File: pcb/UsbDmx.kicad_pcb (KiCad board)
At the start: 2 copper layers, 100 x 100 mm, 101 parts, among them CON101 10PIN_ISP_AVR, CON201 XLR3_F_GROUND, CON202 XLR3_M_GROUND, J101 USB_B, J102 Barrel_Jack, Q201 BC817, Q202 BC817, Q203 BC807, Q204 BC817, Q205 BC817, U101 74LS573, U102 USBN9604-28M, U103 AS6C6264, U104 L7805, U105 ATMEGA8515-16AU, U106 USBLC6-2SC6, U201 SN75176, U202 6N137, U203 6N137, U204 AM2D-0505SZ, U205 SN75176, Y101 24MHz

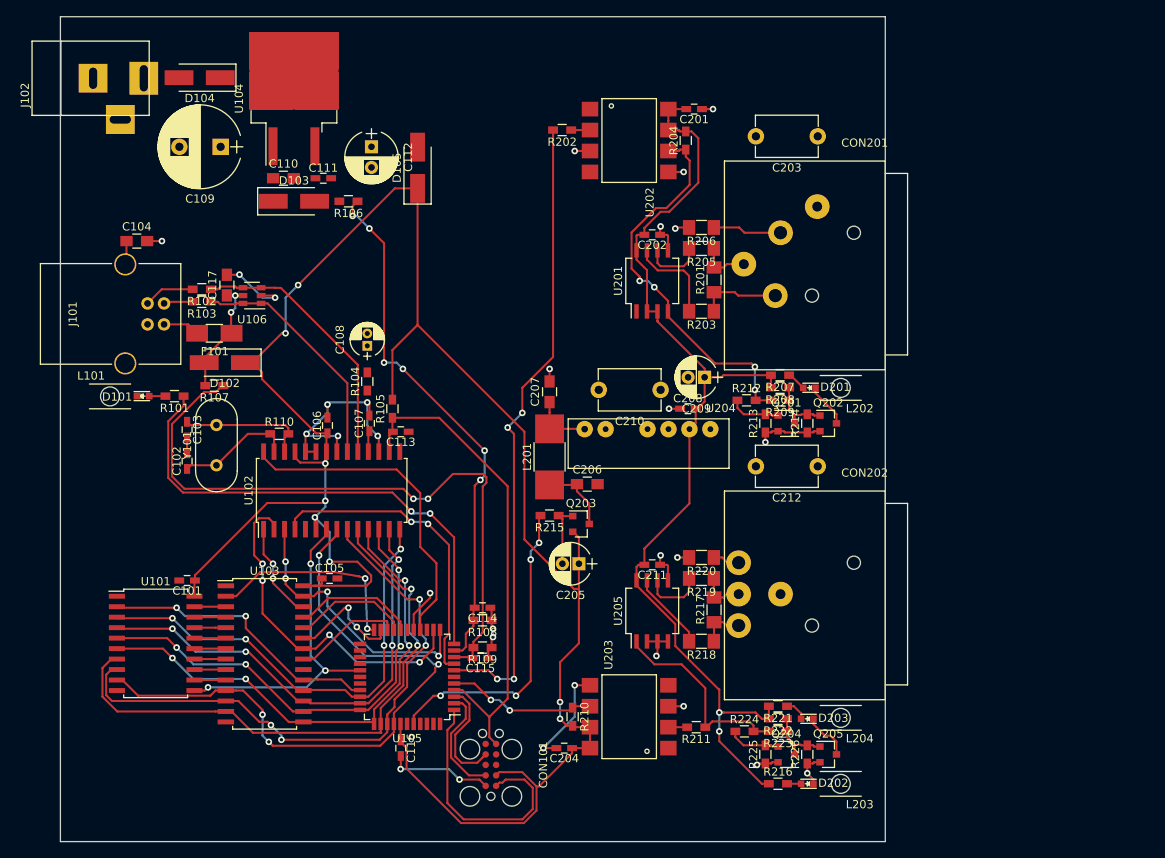
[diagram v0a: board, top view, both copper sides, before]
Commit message: Finished layout
Added esd protection diodes to the dmx interface
Routed everything
added ground planes
added some logos...
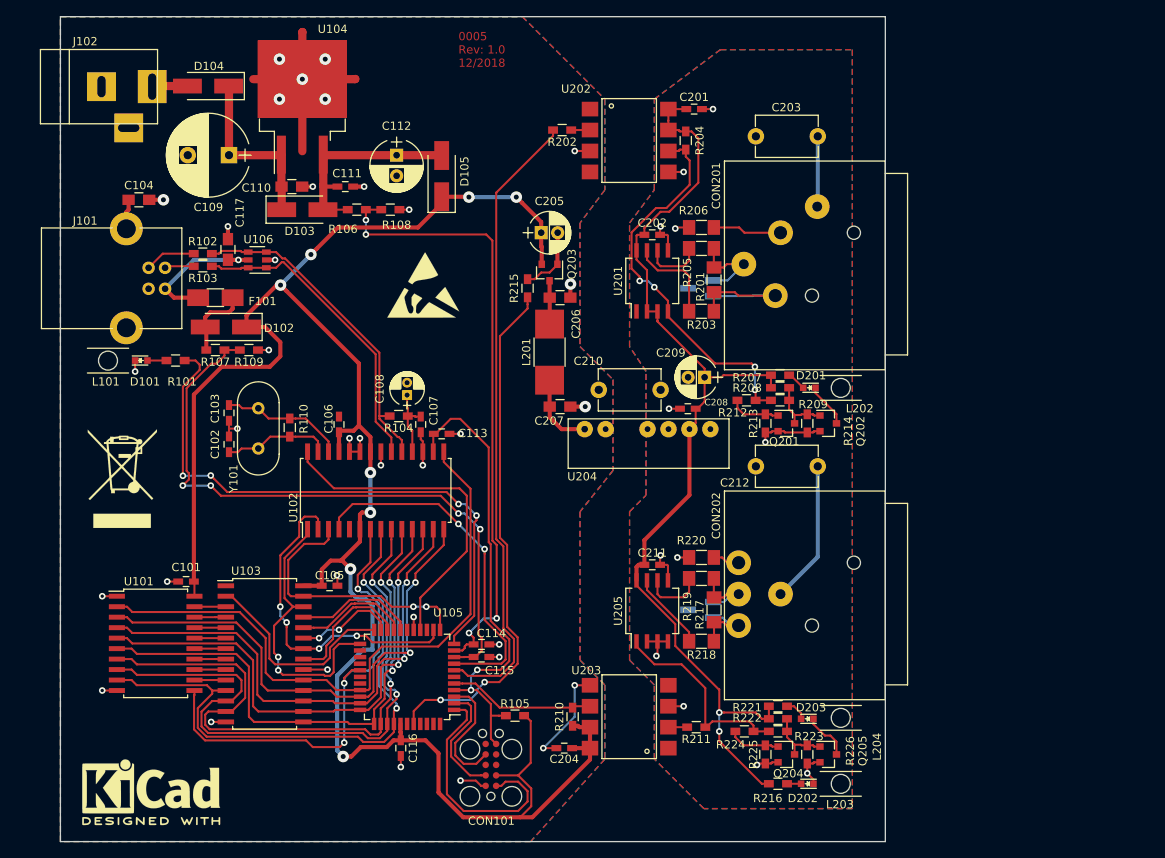
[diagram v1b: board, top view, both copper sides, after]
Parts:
- added G***: LOGO, proz_logo:Shimatta_SolderMask, F.Cu at (89.8, 160.0)
- added REF***: WEEE-Logo_8.4x12mm_SilkScreen, Symbols:WEEE-Logo_8.4x12mm_SilkScreen, F.Cu at (62.5, 121.0)
- added REF***: ESD-Logo_8.9x8mm_SilkScreen, Symbols:ESD-Logo_8.9x8mm_SilkScreen, F.Cu at (99.0, 97.5)
- added REF***: KiCad-Logo2_8mm_SilkScreen, Symbols:KiCad-Logo2_8mm_SilkScreen, F.Cu at (66.0, 159.0)
- added U206: PESD5V0S2BT, TO_SOT_Packages_SMD:SOT-23_Handsoldering, B.Cu at (132.6, 97.9)
- added U207: PESD5V0S2BT, TO_SOT_Packages_SMD:SOT-23_Handsoldering, B.Cu at (132.6, 136.9)
- moved R108 51.0 mm to (95.0, 88.4)
- moved R109 45.9 mm to (77.9, 105.4)
- moved C205 40.4 mm to (113.3, 91.2), turned to 0 degrees
- moved R105 40.1 mm to (110.1, 149.7), turned to 0 degrees
- moved Q203 30.7 mm to (114.3, 96.0), turned to 270 degrees
- moved R215 27.7 mm to (111.6, 97.9), turned to 270 degrees
- moved C206 22.8 mm to (115.6, 99.1)
- moved L201 12.7 mm to (114.3, 105.7), turned to 270 degrees
- moved C108 7.68 mm to (97.0, 110.9)
- moved C107 6.22 mm to (98.7, 114.4), turned to 270 degrees
- moved R104 5.66 mm to (96.0, 113.4), turned to 180 degrees
- moved C102 5.47 mm to (75.4, 116.8)
- moved C103 5.47 mm to (75.4, 113.0)
- moved Y101 5.47 mm to (79.0, 117.3)
- moved U102 5.33 mm to (93.2, 122.4)
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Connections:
- net Net-(CON201-Pad2) renamed /DmxInOut/TX_B
- net Net-(CON201-Pad3) renamed /DmxInOut/TX_A
- net Net-(CON202-Pad2) renamed /DmxInOut/RX_B
- net Net-(CON202-Pad3) renamed /DmxInOut/RX_A
- C117 pad 1: /5V_USB -> Net-(C117-Pad1)
- F101 pad 2: Net-(F101-Pad2) -> Net-(C117-Pad1)
- J101 pad 1: Net-(F101-Pad2) -> Net-(C117-Pad1)
- U106 pad 5: /5V_USB -> Net-(C117-Pad1)
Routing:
- net /AD7: track 34.1 -> 76.5 mm, vias 2 -> 0
- net /5V_EXT: track 0.00 -> 25.9 mm
- net /DmxInOut/DMX_EN: track 37.8 -> 63.5 mm, vias 4 -> 2
- net /A13: track 11.9 -> 34.5 mm
- net Net-(C109-Pad1): track 0.00 -> 21.5 mm
- net /ALE: track 39.8 -> 57.9 mm
- net Net-(C212-Pad1): track 0.00 -> 17.4 mm
- net Net-(C117-Pad1): track 0.00 -> 17.3 mm, vias 0 -> 1
- net GND: track 81.8 -> 93.4 mm, vias 17 -> 35
- net /SENSE_5V_EXT: track 64.6 -> 75.0 mm, vias 6 -> 4
- net /LED_USB: track 61.2 -> 70.6 mm, vias 2 -> 4
- net Net-(C203-Pad1): track 0.00 -> 8.54 mm
- net Net-(R103-Pad1): track 29.0 -> 37.5 mm
- net /DmxInOut/TX_B: track 9.92 -> 17.5 mm
- net Net-(R102-Pad1): track 32.4 -> 40.0 mm
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- added copper zone on B.Cu, net GND
- added copper zone on F.Cu, net GND
- added copper zone on B.Cu, net GNDA
- added copper zone on F.Cu, net GNDA
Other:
- net class Shield added: clearance 4, trace_width 0.25, via_dia 0.8, via_drill 0.4
- board text added: "0005 Rev: 1.0 12/2018"

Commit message: final release 1.0
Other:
- net class Shield: clearance 4 -> 2

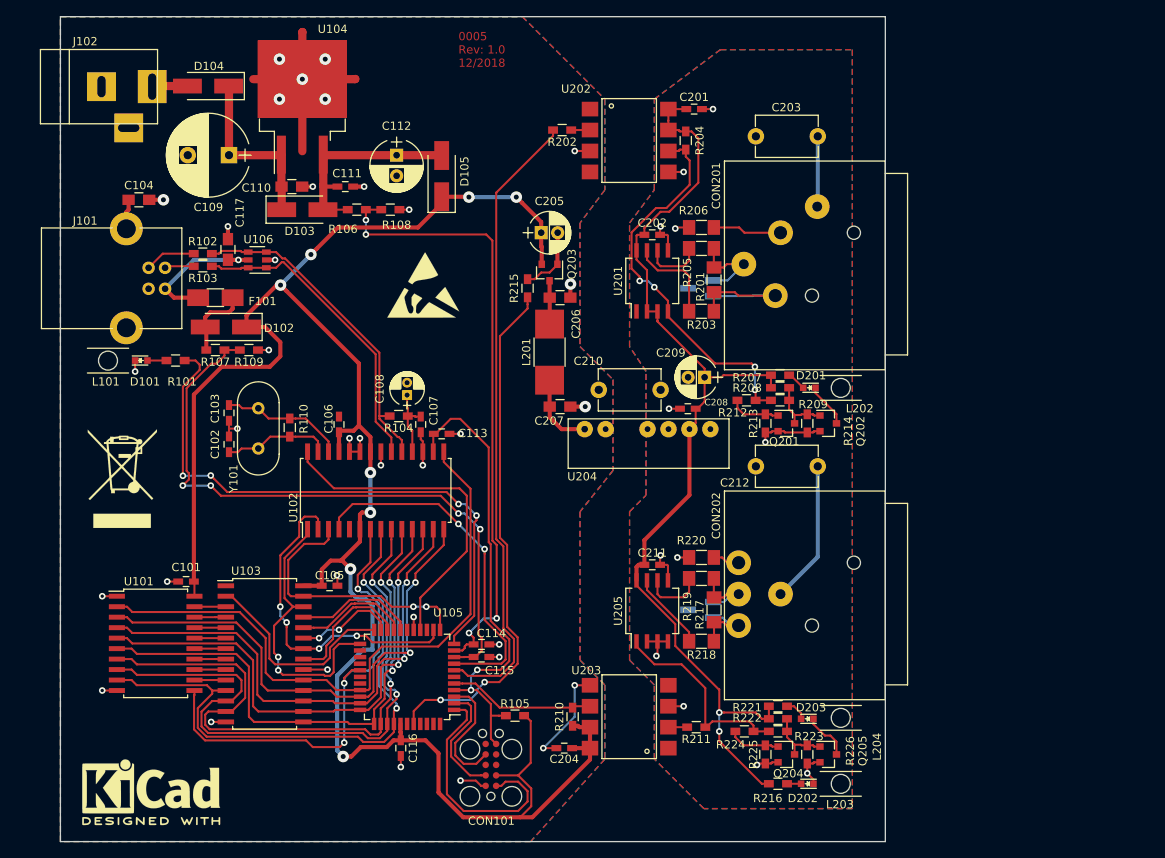
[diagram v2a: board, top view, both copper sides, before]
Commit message: Bugfixing after testing prototype
Added a different pullup mechanism during programming to keep the USBN active during reset. Otherwise the ATmega loses its clock.
Fixed the broken pin association of the DMX connectors.
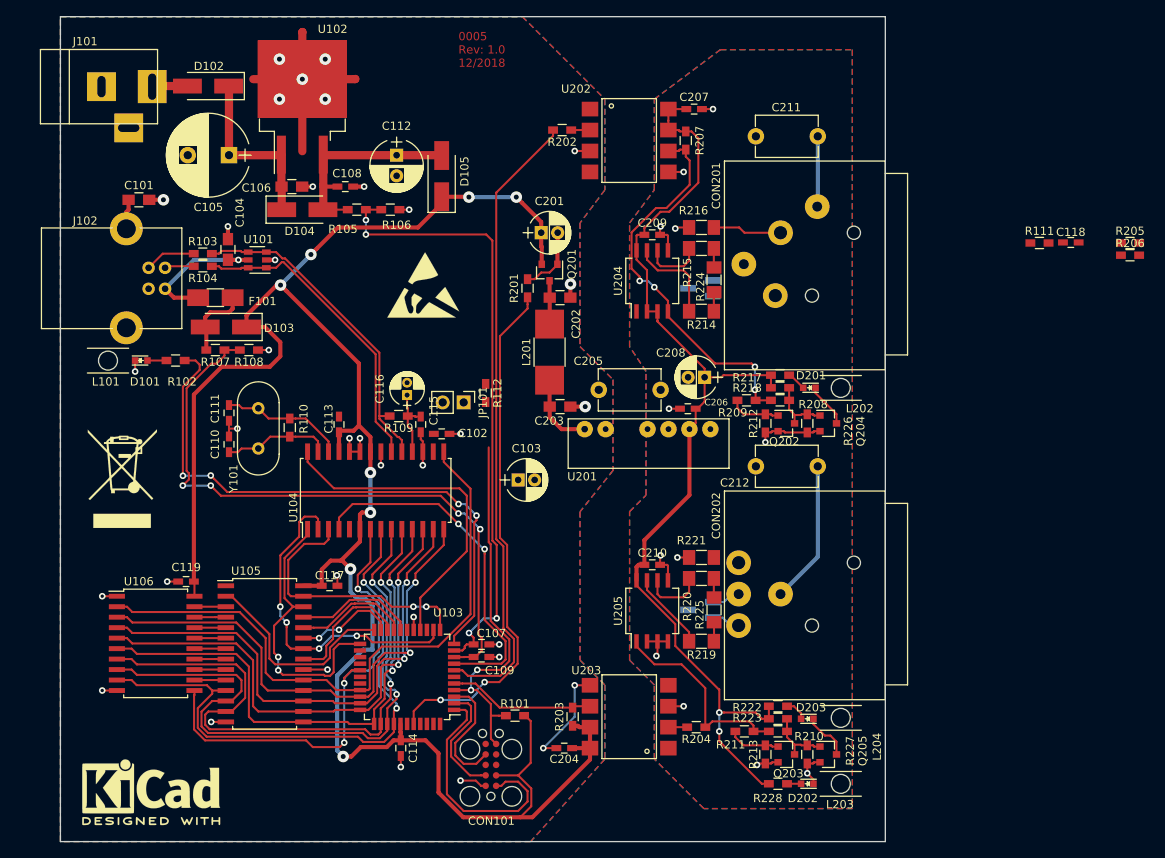
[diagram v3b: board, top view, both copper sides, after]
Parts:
- added C103: 10u, Capacitors_THT:CP_Radial_D5.0mm_P2.00mm, F.Cu at (110.5, 121.2)
- added C118: 100n, Capacitors_SMD:C_0603_HandSoldering, F.Cu at (177.5, 92.4)
- added JP101: programming mode, Pin_Headers:Pin_Header_Straight_1x02_Pitch2.54mm, F.Cu at (103.9, 111.8)
- added R111: 10k, Resistors_SMD:R_0603_HandSoldering, F.Cu at (173.7, 92.4)
- added R112: 1k, Resistors_SMD:R_0603_HandSoldering, F.Cu at (106.6, 110.6)
- added R205: 10k, Resistors_SMD:R_0603_HandSoldering, F.Cu at (184.7, 92.4)
- added R206: 10k, Resistors_SMD:R_0603_HandSoldering, F.Cu at (184.7, 93.9)
- R212: renamed from R213; value 100k -> 47k
- R213: renamed from R225; value 100k -> 47k
- R214: renamed from R203; value 10 -> 1
- R215: renamed from R205; value 10 -> 1
- R226: renamed from R214; value 100k -> 47k
- R227: renamed from R226; value 100k -> 47k
- renumbered C104 to C101, C113 to C102, C117 to C104, C109 to C105, C110 to C106, C114 to C107, C111 to C108, C115 to C109, C102 to C110, C103 to C111, C106 to C113, C116 to C114, C107 to C115, C108 to C116, C105 to C117, C101 to C119, C205 to C201, C206 to C202, C207 to C203, C210 to C205, C208 to C206, C201 to C207, C209 to C208, C202 to C209, C211 to C210, C203 to C211, D104 to D102, D102 to D103, D103 to D104, J102 to J101, J101 to J102, Q203 to Q201, Q201 to Q202, Q204 to Q203, Q202 to Q204, R105 to R101, R101 to R102, R102 to R103, R103 to R104, R106 to R105, R108 to R106, R109 to R108, R104 to R109, R215 to R201, R210 to R203, R211 to R204, R204 to R207, R209 to R208, R212 to R209, R223 to R210, R224 to R211, R206 to R216, R207 to R217, R208 to R218, R218 to R219, R219 to R220, R220 to R221, R221 to R222, R222 to R223, R201 to R224, R217 to R225, R216 to R228, U106 to U101, U104 to U102, U105 to U103, U102 to U104, U103 to U105, U101 to U106, U204 to U201, U201 to U204
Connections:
- CON201 pad 2: /DmxInOut/TX_B -> /DmxInOut/TX_-
- CON201 pad 3: /DmxInOut/TX_A -> /DmxInOut/TX_+
- CON202 pad 2: /DmxInOut/RX_B -> /DmxInOut/RX_-
- CON202 pad 3: /DmxInOut/RX_A -> /DmxInOut/RX_+
- R214 pad 1: /DmxInOut/TX_B -> /DmxInOut/TX_+
- R214 pad 2: Net-(R203-Pad2) -> /DmxInOut/TX_B
- R215 pad 1: /DmxInOut/TX_A -> /DmxInOut/TX_-
- R215 pad 2: Net-(R205-Pad2) -> /DmxInOut/TX_A
- R219 pad 1: /DmxInOut/RX_B -> /DmxInOut/RX_+
- R219 pad 2: Net-(R218-Pad2) -> /DmxInOut/RX_B
- R220 pad 1: /DmxInOut/RX_A -> /DmxInOut/RX_-
- R220 pad 2: Net-(R219-Pad2) -> /DmxInOut/RX_A
- R224 pad 1: /DmxInOut/TX_B -> /DmxInOut/TX_+
- R224 pad 2: /DmxInOut/TX_A -> /DmxInOut/TX_-
- R225 pad 1: /DmxInOut/RX_B -> /DmxInOut/RX_+
- R225 pad 2: /DmxInOut/RX_A -> /DmxInOut/RX_-
- U104 pad 16: /RESET -> /RESET_USBN
- U204 pad 6: Net-(R205-Pad2) -> /DmxInOut/TX_A
- U204 pad 7: Net-(R203-Pad2) -> /DmxInOut/TX_B
- U205 pad 6: Net-(R219-Pad2) -> /DmxInOut/RX_A
- U205 pad 7: Net-(R218-Pad2) -> /DmxInOut/RX_B
- U206 pad 1: /DmxInOut/TX_A -> /DmxInOut/TX_+
- U206 pad 2: /DmxInOut/TX_B -> /DmxInOut/TX_-
- U207 pad 1: /DmxInOut/RX_A -> /DmxInOut/RX_+
- U207 pad 2: /DmxInOut/RX_B -> /DmxInOut/RX_-
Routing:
- net Net-(R203-Pad2): track 11.3 -> 0.00 mm
- net /RESET: track 57.1 -> 46.1 mm
- net Net-(R218-Pad2): track 9.50 -> 0.00 mm
- net Net-(R219-Pad2): track 7.56 -> 0.00 mm
- net Net-(R205-Pad2): track 7.31 -> 0.00 mm
- net /DmxInOut/TX_B: track 17.5 -> 11.3 mm
- net /DmxInOut/RX_+: track 0.00 -> 5.85 mm
- net /DmxInOut/RX_-: track 0.00 -> 5.85 mm
- net /DmxInOut/TX_A: track 10.7 -> 7.31 mm
- net Net-(CON202-Pad1): track 3.27 -> 0.00 mm
- net /DmxInOut/TX_-: track 0.00 -> 2.32 mm
- net /DmxInOut/TX_+: track 0.00 -> 2.32 mm
- net /DmxInOut/RX_A: track 9.00 -> 7.56 mm
- net /DmxInOut/RX_B: track 9.00 -> 9.50 mm

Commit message: fixed XLR connectors, LEDs and Reset
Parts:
- removed the Q202 at (143.0, 114.3)
- removed the Q203 at (143.0, 154.4)
- removed the R205 at (184.7, 92.4)
- removed the R206 at (184.7, 93.9)
- removed the R208 at (142.2, 111.5)
- removed the R209 at (138.2, 111.5)
- removed the R211 at (137.9, 151.6)
- removed the R212 at (140.5, 114.3)
- removed the R213 at (140.5, 154.4)
- removed the R218 at (142.2, 110.0)
- removed R223: 10k, Resistors_SMD:R_0603_HandSoldering
- removed R224: 120, Resistors_SMD:R_MiniMELF_MMA-0204
- removed the U206 at (132.6, 97.9)
- added C205: 100n, Capacitors_SMD:C_0603_HandSoldering, F.Cu at (137.0, 111.3)
- added C206: 100n, Capacitors_SMD:C_0603_HandSoldering, F.Cu at (142.6, 114.6)
- added C215: 100n, Capacitors_SMD:C_0603_HandSoldering, F.Cu at (136.0, 151.1)
- added C216: 100n, Capacitors_SMD:C_0603_HandSoldering, F.Cu at (142.6, 154.7)
- added D202: 1N4148, Diodes_SMD:D_MiniMELF, F.Cu at (140.6, 110.6)
- added D203: 1N4148, Diodes_SMD:D_MiniMELF, F.Cu at (139.1, 114.6)
- added D206: 1N4148, Diodes_SMD:D_MiniMELF, F.Cu at (140.6, 150.6)
- added D207: 1N4148, Diodes_SMD:D_MiniMELF, F.Cu at (139.1, 154.6)
- added R201: 120, Resistors_SMD:R_MiniMELF_MMA-0204, F.Cu at (134.2, 96.9)
- added R219: 1k, Resistors_SMD:R_0603_HandSoldering, F.Cu at (142.7, 153.2)
- added U203: PESD5V0S2BT, TO_SOT_Packages_SMD:SOT-23_Handsoldering, B.Cu at (132.6, 97.9)
- R210: value 10k -> 1k
- moved C114 79.4 mm to (101.5, 115.4), turned to 180 degrees
- moved R107 71.3 mm to (106.3, 115.7), turned to 90 degrees
- moved R210 38.6 mm to (142.7, 113.0)
- moved C115 33.8 mm to (110.1, 148.2)
- moved R217 8.89 mm to (132.6, 139.4)
- moved R203 7.62 mm to (132.8, 93.1)
- moved R205 7.62 mm to (132.8, 100.7)
- moved R106 4.10 mm to (102.7, 109.1), turned to 0 degrees
- moved U207 3.94 mm to (132.5, 133.0)
- moved R214 3.81 mm to (134.1, 133.1)
- moved R215 3.81 mm to (132.6, 136.9)
- moved R216 3.81 mm to (132.6, 129.3)
- renumbered C119 to C101, C110 to C102, C111 to C103, C101 to C104, C104 to C105, C117 to C106, C113 to C107, C115 to C108, C116 to C109, C105 to C110, C106 to C111, C108 to C112, C112 to C113, C118 to C114, C102 to C115, C103 to C116, C107 to C117, C109 to C118, C114 to C119, C207 to C201, C209 to C202, C211 to C203, C201 to C207, C202 to C208, C203 to C209, C206 to C210, C208 to C211, C205 to C212, C210 to C213, C212 to C214, D103 to D102, D104 to D103, D102 to D104, D202 to D204, D203 to D205, J102 to J101, J101 to J102, L202 to L201, L203 to L202, L201 to L203, Q204 to Q201, Q201 to Q202, Q205 to Q203, R102 to R101, R110 to R102, R109 to R105, R112 to R106, R111 to R107, R101 to R108, R105 to R109, R107 to R110, R106 to R111, R108 to R112, R214 to R203, R207 to R204, R215 to R205, R216 to R206, R217 to R207, R203 to R208, R204 to R209, R226 to R211, R201 to R212, R228 to R213, R225 to R214, R219 to R215, R220 to R216, R221 to R217, R222 to R218, R227 to R220, U106 to U101, U101 to U102, U104 to U103, U105 to U104, U102 to U105, U103 to U106, U204 to U201, U203 to U204, U201 to U205, U205 to U206
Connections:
- Q201 pad 1: Net-(Q202-Pad3) -> Net-(Q201-Pad1)
- Q203 pad 1: Net-(Q203-Pad3) -> Net-(Q203-Pad1)
- R209 pad 1: Net-(R204-Pad1) -> Net-(C215-Pad1)
- R210 pad 1: Net-(Q203-Pad3) -> Net-(Q201-Pad1)
- R210 pad 2: Net-(R204-Pad1) -> Net-(C206-Pad2)
- R211 pad 2: Net-(Q202-Pad3) -> Net-(Q201-Pad1)
- R220 pad 2: Net-(Q203-Pad3) -> Net-(Q203-Pad1)
- U206 pad 1: Net-(R204-Pad1) -> Net-(C215-Pad1)
- U207 pad 1: /DmxInOut/RX_+ -> /DmxInOut/RX_-
- U207 pad 2: /DmxInOut/RX_- -> /DmxInOut/RX_+
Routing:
- net GND: track 93.4 -> 128.4 mm, vias 35 -> 37
- net Net-(R204-Pad1): track 24.7 -> 0.00 mm
- net Net-(C215-Pad1): track 0.00 -> 17.6 mm
- net /DmxInOut/TX_-: track 2.32 -> 17.5 mm
- net /RESET_USBN: track 0.00 -> 11.8 mm
- net +5V: track 242.1 -> 252.6 mm, vias 8 -> 10
- net GNDA: track 36.7 -> 26.3 mm, vias 12 -> 10
- net /DmxInOut/TX_+: track 2.32 -> 10.7 mm
- net Net-(Q203-Pad3): track 7.88 -> 0.00 mm
- net Net-(Q202-Pad3): track 7.77 -> 0.00 mm
- net Net-(Q202-Pad1): track 6.24 -> 0.00 mm
- net /RESET: track 46.1 -> 52.2 mm, vias 2 -> 3
- net Net-(C215-Pad2): track 0.00 -> 5.64 mm
- net Net-(C205-Pad1): track 47.7 -> 42.5 mm
- net Net-(C205-Pad2): track 0.00 -> 4.67 mm
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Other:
- board text added: "0005 Rev: 1.1 01/2019"
- board text removed: "0005 Rev: 1.0 12/2018"
